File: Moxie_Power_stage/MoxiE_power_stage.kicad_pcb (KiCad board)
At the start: 4 copper layers, 100 x 60 mm, 147 parts, among them J101 Conn_02x13_Counter_Clockwise, J201 Conn_01x02, J202 Conn_01x02, P101 PHASE_3, P102 PHASE_3, P103 PHASE_1, P104 PHASE_2, P105 PHASE_3, Q301 TPH2R608NH,L1Q, Q302 TPH2R608NH,L1Q, Q303 TPH2R608NH,L1Q, Q304 TPH2R608NH,L1Q, Q305 TPH2R608NH,L1Q, Q306 TPH2R608NH,L1Q, Q401 TPH2R608NH,L1Q, Q402 TPH2R608NH,L1Q, Q403 TPH2R608NH,L1Q, Q404 TPH2R608NH,L1Q, Q405 TPH2R608NH,L1Q, Q406 TPH2R608NH,L1Q, Q501 TPH2R608NH,L1Q, Q502 TPH2R608NH,L1Q, Q503 TPH2R608NH,L1Q, Q504 TPH2R608NH,L1Q, Q505 TPH2R608NH,L1Q, Q506 TPH2R608NH,L1Q, U201 SY8502, U301 MIC4605-1YMT, U302 ACS711, U401 MIC4605-1YMT, U402 ACS711, U501 MIC4605-1YMT, U502 ACS711

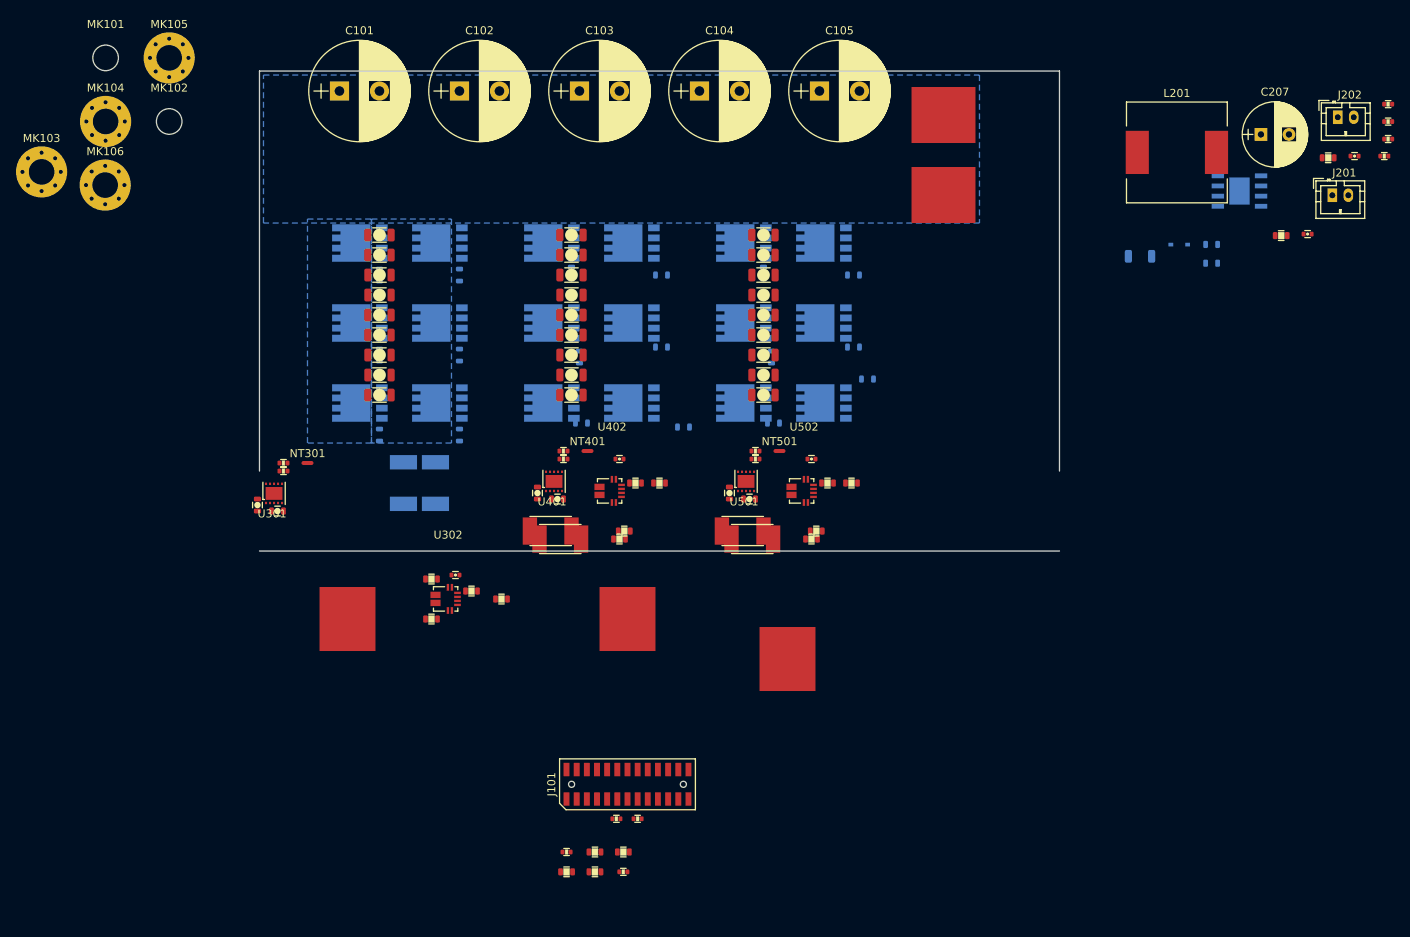
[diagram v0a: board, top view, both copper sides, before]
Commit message: attempt at a 2 layer power stage pcb with some caveats. unfinished
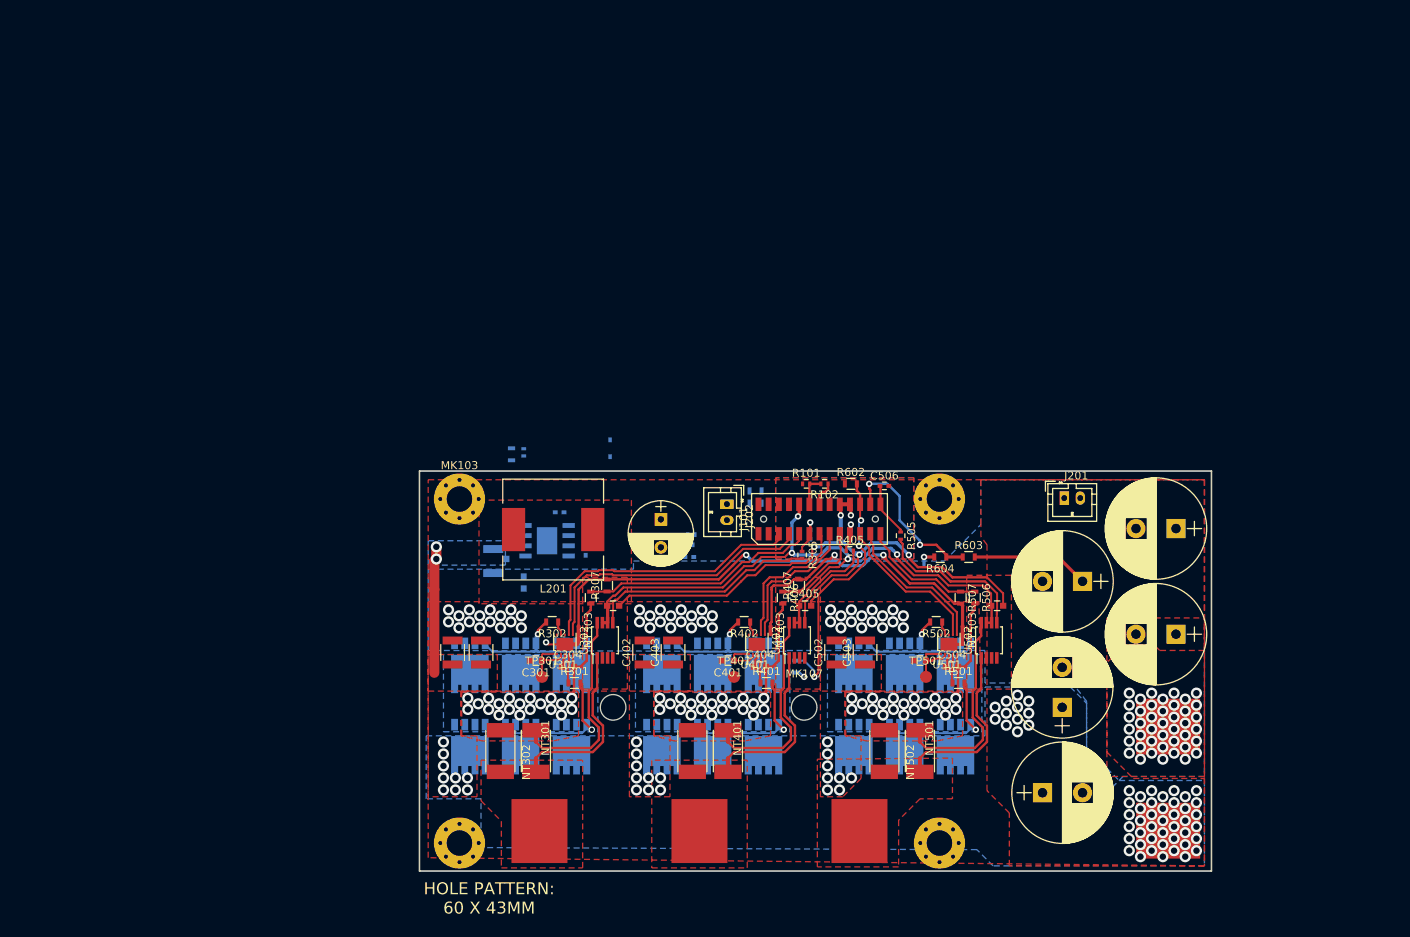
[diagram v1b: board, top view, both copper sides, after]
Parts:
- removed C307, C308, C309, C311, C407, C408, C409, C411, C507, C508, C509, C511: 100v_1.0uF, pkl_dipol:C_1206
- removed C310, C410, C510: 1uf, pkl_dipol:C_0603
- removed C315, C415, C515: 2.2u, pkl_dipol:C_0402
- removed MK105: Mounting_Hole, Mounting_Holes:MountingHole_3.2mm_M3_Pad_Via
- removed R308, R408, R508: 10R, pkl_dipol:R_0603
- removed R309, R312, R409, R412, R509, R512: 1.0mΩ, pkl_dipol:R_0603
- removed R310, R410, R510: 0.5mΩ, moxie-drive-custom:R_2512_shunt_vishay
- removed R311, R411, R511: 1.0mΩ, moxie-drive-custom:R_2512_shunt_vishay
- removed R313, R413, R513: 39k, pkl_dipol:R_0603
- removed R314, R414, R514: 2k2, pkl_dipol:R_0603
- added MK107: Mounting_Hole, Mounting_Holes:MountingHole_3.2mm_M3, F.Cu at (148.1, 129.5)
- added NT302: Net-Tie_2, NetTie:NetTie-2_SMD_Pad0.5mm, F.Cu at (114.6, 136.4)
- added NT303: Net-Tie_2, NetTie:NetTie-2_SMD_Pad0.5mm, F.Cu at (119.9, 119.9)
- added NT402: Net-Tie_2, NetTie:NetTie-2_SMD_Pad0.5mm, F.Cu at (138.6, 136.4)
- added NT403: Net-Tie_2, NetTie:NetTie-2_SMD_Pad0.5mm, F.Cu at (143.9, 119.9)
- added NT502: Net-Tie_2, NetTie:NetTie-2_SMD_Pad0.5mm, F.Cu at (162.6, 136.4)
- added NT503: Net-Tie_2, NetTie:NetTie-2_SMD_Pad0.5mm, F.Cu at (167.9, 119.9)
- added TP301: Test_Point, Measurement_Points:Measurement_Point_Round-SMD-Pad_Small, F.Cu at (115.3, 125.7)
- added TP401: Test_Point, Measurement_Points:Measurement_Point_Round-SMD-Pad_Small, F.Cu at (139.3, 125.7)
- added TP501: Test_Point, Measurement_Points:Measurement_Point_Round-SMD-Pad_Small, F.Cu at (163.3, 125.7)
- C201: footprint pkl_dipol:C_1206 -> Capacitors_SMD:C_1210
- C202, C206, C301, C401, C501: footprint pkl_dipol:C_0603 -> Capacitors_SMD:C_0603
- C203: footprint pkl_dipol:R_0402 -> Capacitors_SMD:C_0402; moved to B.Cu
- C204, C205: footprint pkl_dipol:C_0402 -> Capacitors_SMD:C_0402; moved to B.Cu
- C302, C303, C402, C403, C502, C503: value 100v_1.0uF -> 100v_2.2uF; footprint pkl_dipol:C_1206 -> Capacitors_SMD:C_1210
- C304, C404, C504: value 100v_1.0uF -> 1uf; footprint pkl_dipol:C_1206 -> Capacitors_SMD:C_0603
- C305, C405, C505: value 100v_1.0uF -> 2.2uf; footprint pkl_dipol:C_1206 -> Capacitors_SMD:C_0603
- C306, C406: value 100v_1.0uF -> C; footprint pkl_dipol:C_1206 -> Capacitors_SMD:C_0402; moved to B.Cu
- C506: value 100v_1.0uF -> C; footprint pkl_dipol:C_1206 -> Capacitors_SMD:C_0402
- MK101, MK102: footprint Mounting_Holes:MountingHole_3.2mm_M3 -> Mounting_Holes:MountingHole_3.2mm_M3_Pad_Via
- MK106: footprint Mounting_Holes:MountingHole_3.2mm_M3_Pad_Via -> Mounting_Holes:MountingHole_3.2mm_M3
- R101, R102: footprint pkl_dipol:R_0402 -> Resistors_SMD:R_0402
- R201, R203, R605, R606: footprint pkl_dipol:R_0603 -> Resistors_SMD:R_0603; moved to B.Cu
- R202, R204, R205: footprint pkl_dipol:R_0402 -> Resistors_SMD:R_0402; moved to B.Cu
- R301, R302, R401, R402, R501, R502: value 2k2 -> 10R; footprint pkl_dipol:R_0402 -> Resistors_SMD:R_0603
- R303, R304, R403, R404, R503, R504: value 10R -> 300u-Ohm; footprint pkl_dipol:R_0603 -> moxie-drive-custom:R_2512_shunt_vishay; moved to F.Cu
- R305, R405, R505: value 10R -> 0; footprint pkl_dipol:R_0603 -> Resistors_SMD:R_0402; moved to F.Cu
- R306, R406, R506: value 10R -> 39k; footprint pkl_dipol:R_0603 -> Resistors_SMD:R_0603; moved to F.Cu
- R307, R407, R507: value 10R -> 2k2; footprint pkl_dipol:R_0603 -> Resistors_SMD:R_0603; moved to F.Cu
- R601: value 10k -> 10k ntc; footprint pkl_dipol:R_0402 -> Resistors_SMD:R_0603; moved to B.Cu
- R602: value 10k ntc -> 10k; footprint pkl_dipol:R_0402 -> Resistors_SMD:R_0603
- R603, R604: footprint pkl_dipol:R_0603 -> Resistors_SMD:R_0603
- U302, U402, U502: value ACS711 -> AD8418; footprint Mas_custom_parts:ACS711KEX -> Housings_SSOP:MSOP-8_3x3mm_Pitch0.65mm
- moved MK102 131.9 mm to (165.0, 146.5)
- moved C101 118.7 mm to (180.3, 129.5), turned to 90 degrees
- moved R202 116.5 mm to (113.0, 97.7), turned to 90 degrees
- moved MK104 114.4 mm to (165.0, 103.5)
- moved C102 114.0 mm to (177.9, 140.2)
- moved R203 112.6 mm to (111.1, 107.4), turned to 90 degrees
- moved C203 112.3 mm to (117.5, 105.2), turned to 180 degrees
- moved C204 108.0 mm to (120.8, 110.0), turned to 270 degrees
- moved MK101 107.7 mm to (105.0, 146.5)
- moved R204 102.1 mm to (133.7, 109.2), turned to 180 degrees
- moved C103 100.8 mm to (194.6, 120.4), turned to 180 degrees
- moved R205 100.2 mm to (134.0, 108.0)
- moved R201 100.0 mm to (111.5, 97.9), turned to 90 degrees
- moved U201 97.0 mm to (116.0, 108.7)
- moved C202 96.2 mm to (110.9, 110.2), turned to 270 degrees
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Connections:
- C304 pad 1: VBUS -> Net-(C304-Pad1)
- C304 pad 2: GNDPWR -> /phaseA/PHASE_R
- C305 pad 1: VBUS -> /FAULT_RESET
- C305 pad 2: GNDPWR -> GNDA
- C306 pad 1: VBUS -> /PHASE_CURRENT_1_ADC
- C306 pad 2: GNDPWR -> GNDA
- C404 pad 1: VBUS -> Net-(C404-Pad1)
- C404 pad 2: GNDPWR -> /phaseB/PHASE_R
- C405 pad 1: VBUS -> /FAULT_RESET
- C405 pad 2: GNDPWR -> GNDA
- C406 pad 1: VBUS -> /PHASE_CURRENT_2_ADC
- C406 pad 2: GNDPWR -> GNDA
- C504 pad 1: VBUS -> Net-(C504-Pad1)
- C504 pad 2: GNDPWR -> /phaseC/PHASE_R
- C505 pad 1: VBUS -> /FAULT_RESET
- C505 pad 2: GNDPWR -> GNDA
- C506 pad 1: VBUS -> /PHASE_CURRENT_3_ADC
- C506 pad 2: GNDPWR -> GNDA
- NT301 pad 1: GND -> /phaseA/PHASE_R
- NT301 pad 2: GNDPWR -> Net-(NT301-Pad2)
- NT401 pad 1: GND -> /phaseB/PHASE_R
- NT401 pad 2: GNDPWR -> Net-(NT401-Pad2)
- NT501 pad 1: GND -> /phaseC/PHASE_R
- NT501 pad 2: GNDPWR -> Net-(NT501-Pad2)
- Q301 pad 2: Net-(Q301-Pad2) -> /phaseA/HG_R
- Q302 pad 2: Net-(Q302-Pad2) -> /phaseA/LG_R
- Q303 pad 2: Net-(Q303-Pad2) -> /phaseA/HG_R
- Q304 pad 2: Net-(Q304-Pad2) -> /phaseA/LG_R
- Q305 pad 2: Net-(Q305-Pad2) -> /phaseA/HG_R
- Q306 pad 2: Net-(Q306-Pad2) -> /phaseA/LG_R
- Q401 pad 2: Net-(Q401-Pad2) -> /phaseB/HG_R
- Q402 pad 2: Net-(Q402-Pad2) -> /phaseB/LG_R
- Q403 pad 2: Net-(Q403-Pad2) -> /phaseB/HG_R
- Q404 pad 2: Net-(Q404-Pad2) -> /phaseB/LG_R
- Q405 pad 2: Net-(Q405-Pad2) -> /phaseB/HG_R
- Q406 pad 2: Net-(Q406-Pad2) -> /phaseB/LG_R
- Q501 pad 2: Net-(Q501-Pad2) -> /phaseC/HG_R
- Q502 pad 2: Net-(Q502-Pad2) -> /phaseC/LG_R
- Q503 pad 2: Net-(Q503-Pad2) -> /phaseC/HG_R
- Q504 pad 2: Net-(Q504-Pad2) -> /phaseC/LG_R
- Q505 pad 2: Net-(Q505-Pad2) -> /phaseC/HG_R
- Q506 pad 2: Net-(Q506-Pad2) -> /phaseC/LG_R
- R301 pad 1: /L1 -> /phaseA/HG
- R301 pad 2: GND -> /phaseA/HG_R
- R302 pad 1: /H1 -> /phaseA/LG
- R302 pad 2: GND -> /phaseA/LG_R
- R303 pad 1: Net-(Q302-Pad2) -> /phaseA/PHASE_OUT
- R303 pad 2: /phaseA/LG -> /phaseA/PHASE_R
- R304 pad 1: Net-(Q301-Pad2) -> /phaseA/PHASE_OUT
- R304 pad 2: /phaseA/HG -> /phaseA/PHASE_R
- R305 pad 1: Net-(Q303-Pad2) -> /PHASE_CURRENT_1_ADC
- R305 pad 2: /phaseA/HG -> /phaseA/PHASE_I_R
- R306 pad 1: Net-(Q304-Pad2) -> /PHASE_V_1_ADC
- R306 pad 2: /phaseA/LG -> /phaseA/PHASE_R
- R307 pad 1: Net-(Q305-Pad2) -> /PHASE_V_1_ADC
- R307 pad 2: /phaseA/HG -> GND
- R401 pad 1: /L2 -> /phaseB/HG
- R401 pad 2: GND -> /phaseB/HG_R
- R402 pad 1: /H2 -> /phaseB/LG
- R402 pad 2: GND -> /phaseB/LG_R
- R403 pad 1: Net-(Q402-Pad2) -> /phaseB/PHASE_OUT
- R403 pad 2: /phaseB/LG -> /phaseB/PHASE_R
- R404 pad 1: Net-(Q401-Pad2) -> /phaseB/PHASE_OUT
- R404 pad 2: /phaseB/HG -> /phaseB/PHASE_R
- R405 pad 1: Net-(Q403-Pad2) -> /PHASE_CURRENT_2_ADC
- R405 pad 2: /phaseB/HG -> /phaseB/PHASE_I_R
- R406 pad 1: Net-(Q404-Pad2) -> /PHASE_V_2_ADC
- R406 pad 2: /phaseB/LG -> /phaseB/PHASE_R
- R407 pad 1: Net-(Q405-Pad2) -> /PHASE_V_2_ADC
- R407 pad 2: /phaseB/HG -> GND
- R501 pad 1: /L3 -> /phaseC/HG
- R501 pad 2: GND -> /phaseC/HG_R
- R502 pad 1: /H3 -> /phaseC/LG
- R502 pad 2: GND -> /phaseC/LG_R
- R503 pad 1: Net-(Q502-Pad2) -> /phaseC/PHASE_OUT
- R503 pad 2: /phaseC/LG -> /phaseC/PHASE_R
- R504 pad 1: Net-(Q501-Pad2) -> /phaseC/PHASE_OUT
- R504 pad 2: /phaseC/HG -> /phaseC/PHASE_R
- R505 pad 1: Net-(Q503-Pad2) -> /PHASE_CURRENT_3_ADC
- R505 pad 2: /phaseC/HG -> /phaseC/PHASE_I_R
- R506 pad 1: Net-(Q504-Pad2) -> /PHASE_V_3_ADC
- R506 pad 2: /phaseC/LG -> /phaseC/PHASE_R
- R507 pad 1: Net-(Q505-Pad2) -> /PHASE_V_3_ADC
- R507 pad 2: /phaseC/HG -> GND
- R601 pad 1: /FAULT_RESET -> GNDA
- R602 pad 1: GNDA -> /FAULT_RESET
- U201 pad 1: GNDPWR -> (no net)
- U301 pad 1: /EN_GATE -> 12v_buck_vout
- U301 pad 3: Net-(C310-Pad1) -> Net-(C304-Pad1)
- U302 pad 2: Net-(R312-Pad1) -> GNDA
- U302 pad 5: GND -> /phaseA/PHASE_I_R
- U302 pad 6: /FAULT -> /FAULT_RESET
- U401 pad 1: /EN_GATE -> 12v_buck_vout
- U401 pad 3: Net-(C410-Pad1) -> Net-(C404-Pad1)
- U402 pad 2: Net-(R412-Pad1) -> GNDA
- U402 pad 5: GND -> /phaseB/PHASE_I_R
- U402 pad 6: /FAULT -> /FAULT_RESET
- U501 pad 1: /EN_GATE -> 12v_buck_vout
- U501 pad 3: Net-(C510-Pad1) -> Net-(C504-Pad1)
- U502 pad 2: Net-(R512-Pad1) -> GNDA
- U502 pad 5: GND -> /phaseC/PHASE_I_R
- U502 pad 6: /FAULT -> /FAULT_RESET
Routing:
- net /FAULT_RESET: track 0.00 -> 81.4 mm, vias 0 -> 4
- net GND: track 0.00 -> 77.8 mm, vias 0 -> 3
- net GNDA: track 0.00 -> 77.4 mm, vias 0 -> 6
- net /H1: track 0.00 -> 36.1 mm
- net /L1: track 0.00 -> 35.5 mm
- net /FET_TEMP_SENSE: track 0.00 -> 32.1 mm, vias 0 -> 3
- net VBUS: track 0.00 -> 30.6 mm, vias 0 -> 82
- net /PHASE_V_1_ADC: track 0.00 -> 29.6 mm
- net /phaseA/PHASE_I_R: track 0.00 -> 28.5 mm
- net Net-(NT501-Pad2): track 0.00 -> 24.2 mm
- net Net-(NT401-Pad2): track 0.00 -> 24.2 mm
- net Net-(NT301-Pad2): track 0.00 -> 24.2 mm
- net /phaseA/HG_R: track 0.00 -> 23.9 mm, vias 0 -> 1
- net /phaseC/HG_R: track 0.00 -> 23.9 mm, vias 0 -> 1
- net /phaseB/HG_R: track 0.00 -> 23.9 mm, vias 0 -> 1
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- added copper zone on F.Cu, net (none)
- added copper zone on F.Cu, net /phaseA/PHASE_OUT
- added copper zone on F.Cu, net /phaseA/PHASE_R
- added copper zone on F.Cu, net /phaseB/PHASE_OUT
- added copper zone on B.Cu, net /phaseB/PHASE_R
- added copper zone on F.Cu, net /phaseB/PHASE_R
- added copper zone on F.Cu, net /phaseC/PHASE_OUT
- added copper zone on B.Cu, net /phaseC/PHASE_R
- added copper zone on F.Cu, net /phaseC/PHASE_R
- added copper zone on B.Cu, net GNDA
- added copper zone on F.Cu, net GNDA
- added copper zone on B.Cu, net GNDPWR
- added copper zone on F.Cu, net GNDPWR
- added copper zone on F.Cu, net VBUS
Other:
- board size 100 x 60 mm -> 99 x 50 mm
- copper layers 4 -> 2
- net class Default: clearance 0.2 -> 0.17; trace_width 0.25 -> 0.2032
- net class Power removed
- net class vbat added: clearance 0.2, trace_width 0.2032, via_dia 0.8, via_drill 0.4
- rule solder_mask_min_width: 0.05 -> 0.25
- rule trace_clearance: 0.2 -> 0.17
- board text added: "EDGE 5MM FROM HOLE"
- board text added: "HOLE PATTERN: 60 X 43MM"
